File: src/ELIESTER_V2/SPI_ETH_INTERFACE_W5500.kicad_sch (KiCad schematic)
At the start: 44 parts, among them J8 RJ45_Bel_SI-60062-F, U12 W5500, U17 SN74AHC1G125, Y2 25MHz

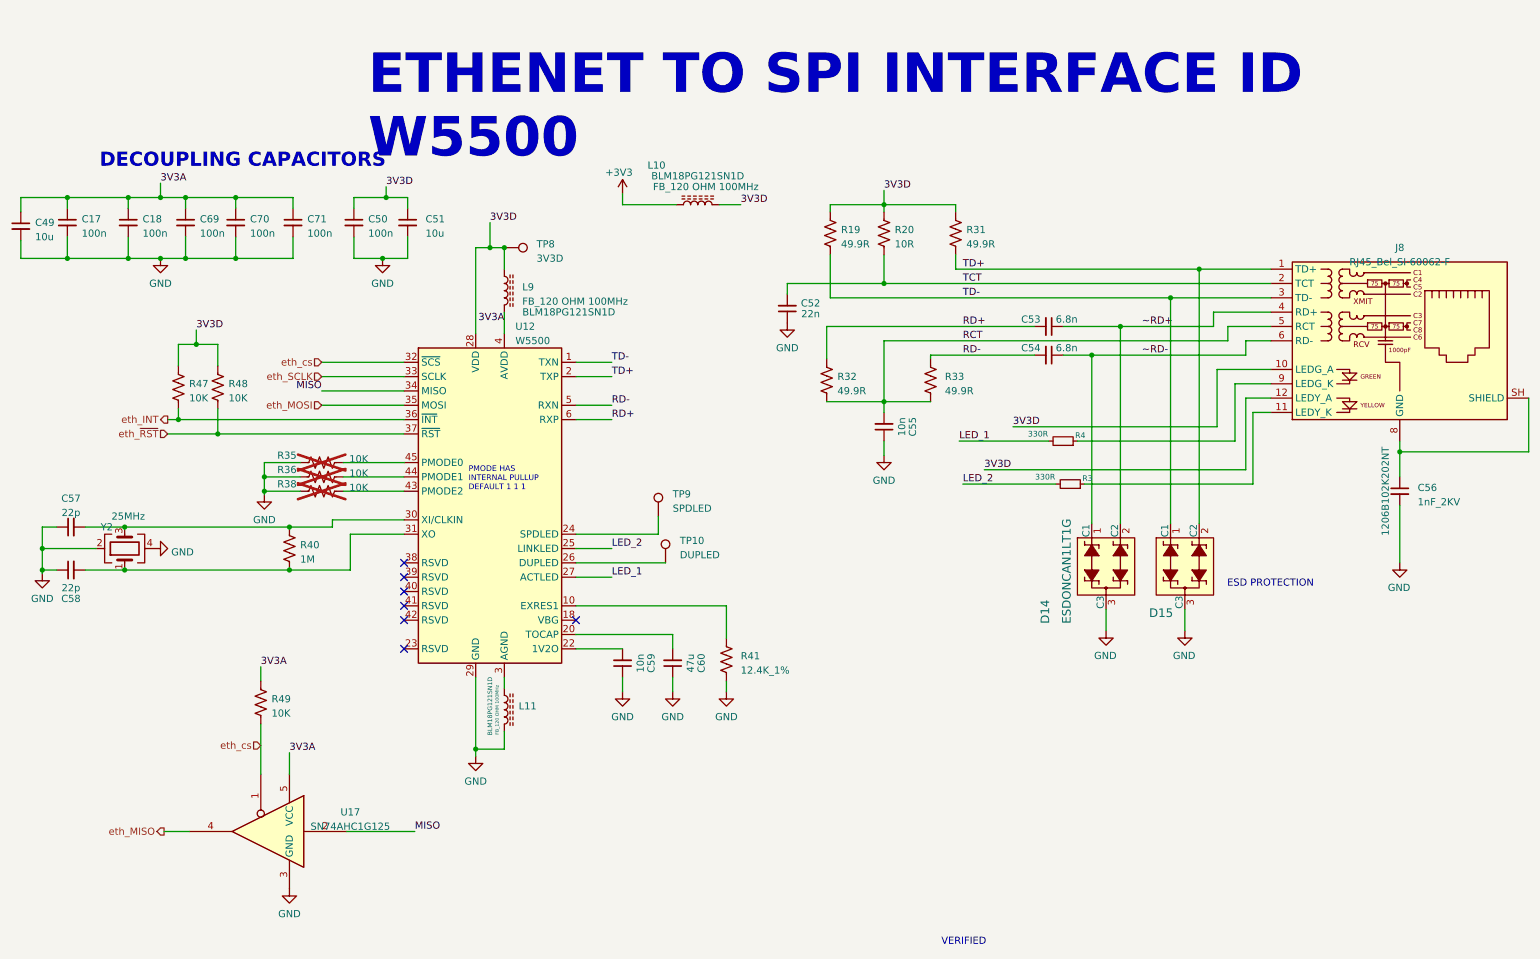
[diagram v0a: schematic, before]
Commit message: update on antenna an LAN side
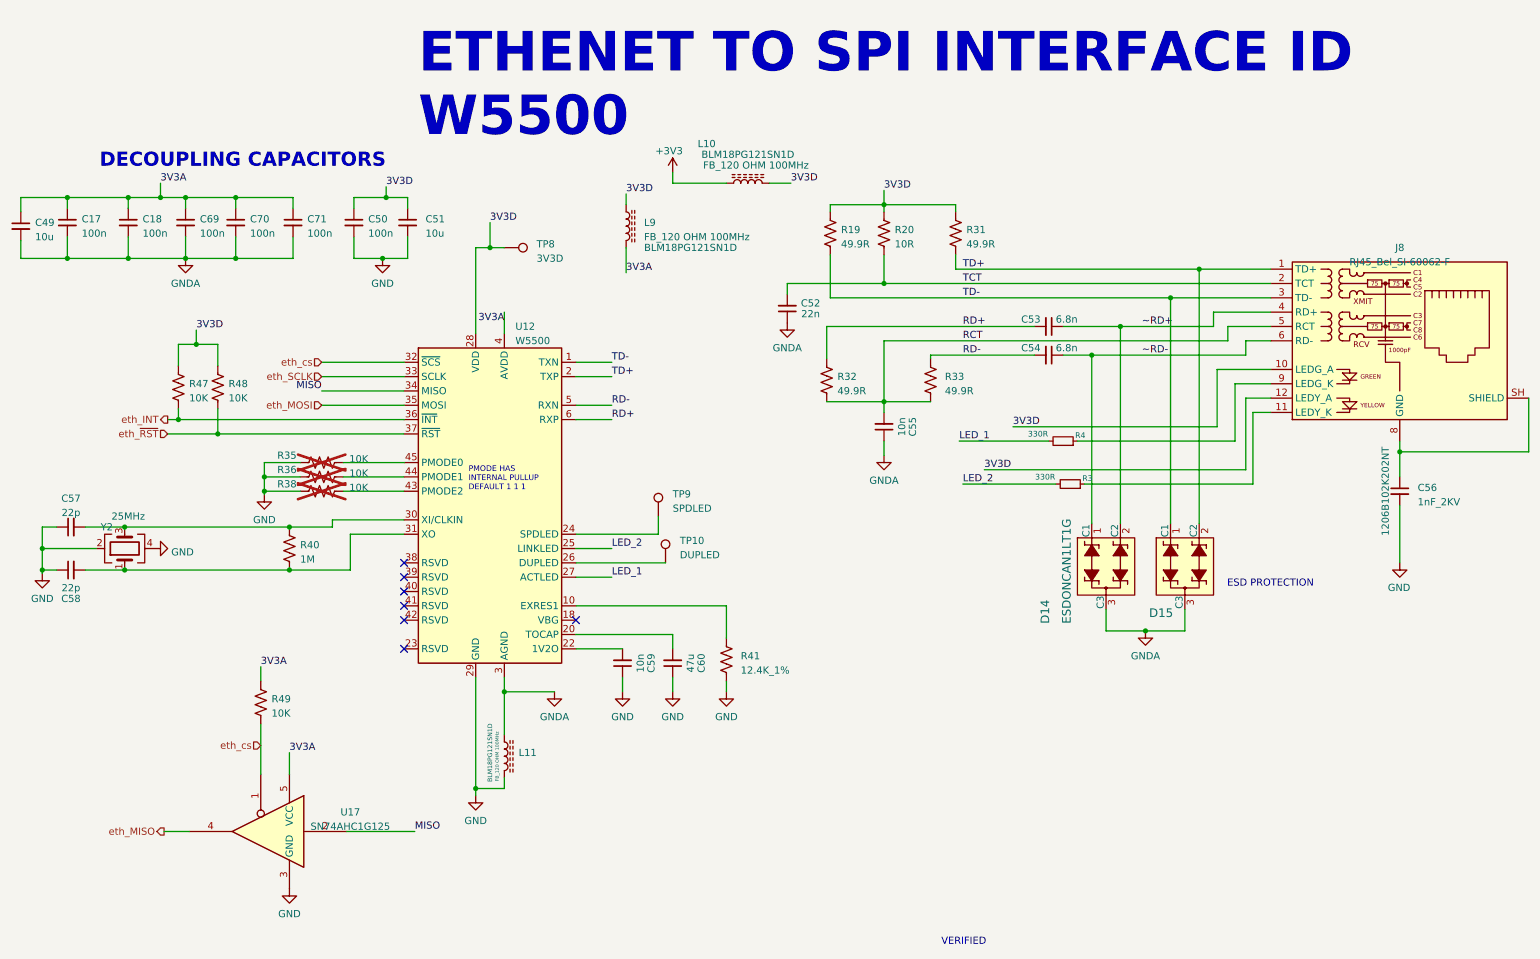
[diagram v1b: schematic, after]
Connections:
- net GND: no longer C17.2, C18.2, C49.2, C52.1, C55.1, C69.2, C70.2, C71.2, D14.3 (C3), D15.3 (C3)
- net GNDA: now reaches L11.1, U12.14 (AGND), U12.16 (AGND), U12.19 (AGND), U12.3 (AGND), U12.48 (AGND), U12.9 (AGND)
- net GNDA: now also C17.2, C18.2, C49.2, C52.1, C55.1, C69.2, C70.2, C71.2, D14.3 (C3), D15.3 (C3)
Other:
- moved on the sheet: L10, L11, L9

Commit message: schematic update and gerber updates with corrections
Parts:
- C57, C58: value 22p -> 16p
- Y2: MPN (none) -> 7M25000013
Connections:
- net 3V3A: no longer R49.2, U17.5 (VCC)
- net 3V3D: now also R49.2, U17.5 (VCC)
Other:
- note added: "LOAD CAPACITANCE = 10P (10-2)*2 = 16P BEST VALUE"
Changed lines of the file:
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@@
+    (effects (font (size 1.27 1.27)) (justify left bottom))
+  )
+  (text "LOAD CAPACITANCE = 10P\n(10-2)*2 = 16P BEST VALUE" (at 15.24 123.825 0)
     (effects (font (size 1.27 1.27)) (justify left bottom))
   )
@@
     (effects (font (size 1.27 1.27)) (justify left bottom))
   )
+  (label "3V3D" (at 62.865 143.51 0) (fields_autoplaced)
+    (effects (font (size 1.27 1.27)) (justify left bottom))
+  )
   (label "RCT" (at 182.245 70.485 0) (fields_autoplaced)
     (effects (font (size 1.27 1.27)) (justify left bottom))
@@
     (effects (font (size 1.27 1.27)) (justify left bottom))
   )
+  (label "3V3D" (at 57.785 128.27 0) (fields_autoplaced)
+    (effects (font (size 1.27 1.27)) (justify left bottom))
+  )
   (label "3V3A" (at 40.005 42.545 0) (fields_autoplaced)
     (effects (font (size 1.27 1.27)) (justify left bottom))
@@
     (effects (font (size 1.27 1.27)) (justify left bottom))
   )
-  (label "3V3A" (at 57.785 128.27 0) (fields_autoplaced)
-    (effects (font (size 1.27 1.27)) (justify left bottom))
-  )
   (label "3V3D" (at 122.555 44.45 0) (fields_autoplaced)
     (effects (font (size 1.27 1.27)) (justify left bottom))
@@
   )
   (label "3V3D" (at 98.425 49.53 0) (fields_autoplaced)
-    (effects (font (size 1.27 1.27)) (justify left bottom))
-  )
-  (label "3V3A" (at 62.865 143.51 0) (fields_autoplaced)
     (effects (font (size 1.27 1.27)) (justify left bottom))
   )
@@
   (symbol (lib_id "Device:Crystal_GND24") (at 33.655 107.315 90) (unit 1)
     (in_bom yes) (on_board yes) (dnp no)
-    (property "Reference" "Y2" (at 30.48 103.505 90)
-      (effects (font (size 1.27 1.27)))
-    )
-    (property "Value" "25MHz" (at 34.29 101.6 90)
+    (property "Reference" "Y2" (at 36.83 102.235 90)
+      (effects (font (size 1.27 1.27)))
+    )
+    (property "Value" "25MHz" (at 31.75 102.235 90)
       (effects (font (size 1.27 1.27)))
     )
@@
     (property "Datasheet" "~" (at 33.655 107.315 0)
       (effects (font (size 1.27 1.27)) hide)
+    )
+    (property "MPN" "7M25000013" (at 33.655 100.33 90)
+      (effects (font (size 1.27 1.27)))
     )
     (pin "1")
@@
   (symbol (lib_id "Device:C_Small") (at 24.13 103.505 90) (unit 1)
     (in_bom yes) (on_board yes) (dnp no) (fields_autoplaced)
-    (property "Reference" "C57" (at 24.1363 98.425 90)
-      (effects (font (size 1.27 1.27)))
-    )
-    (property "Value" "22p" (at 24.1363 100.965 90)
+    (property "Reference" "C57" (at 24.1363 97.79 90)
+      (effects (font (size 1.27 1.27)))
+    )
+    (property "Value" "16p" (at 24.1363 100.33 90)
       (effects (font (size 1.27 1.27)))
     )
@@
       (effects (font (size 1.27 1.27)))
     )
-    (property "Value" "22p" (at 24.13 114.3 90)
-      (effects (font (size 1.27 1.27)))
-    )
+    (property "Value" "16p" (at 24.13 114.3 90)
+      (effects (font (size 1.27 1.27)))
+    )
